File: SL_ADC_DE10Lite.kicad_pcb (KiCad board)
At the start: 4 copper layers, 98 x 67 mm, 23 parts, among them J1 DE10Lite header, J2 Analog header

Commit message: updated?
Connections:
- C5 pad 2: /DGND -> /AGND
- IC1 pad 24: /DGND -> /AGND
- J1 pad 12: /DGND -> /AGND
- J1 pad 30: /DGND -> /AGND
- J2 pad 27: /DGND -> /AGND
- J2 pad 28: /DGND -> /AGND
- J2 pad 5: unconnected-(J2-Pin_5-Pad5) -> /DVDD
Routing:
- net /AGND: track 82.6 -> 160.9 mm, vias 8 -> 26
- net /DGND: track 63.3 -> 0.00 mm, vias 3 -> 0
- net /DVDD: track 25.2 -> 77.2 mm, vias 1 -> 2
- added copper zone on In1.Cu, net /AGND
- removed copper zone on In1.Cu, net /DGND
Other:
- board text added: "DGND 3V3"
- board text removed: "DGND DVDD"

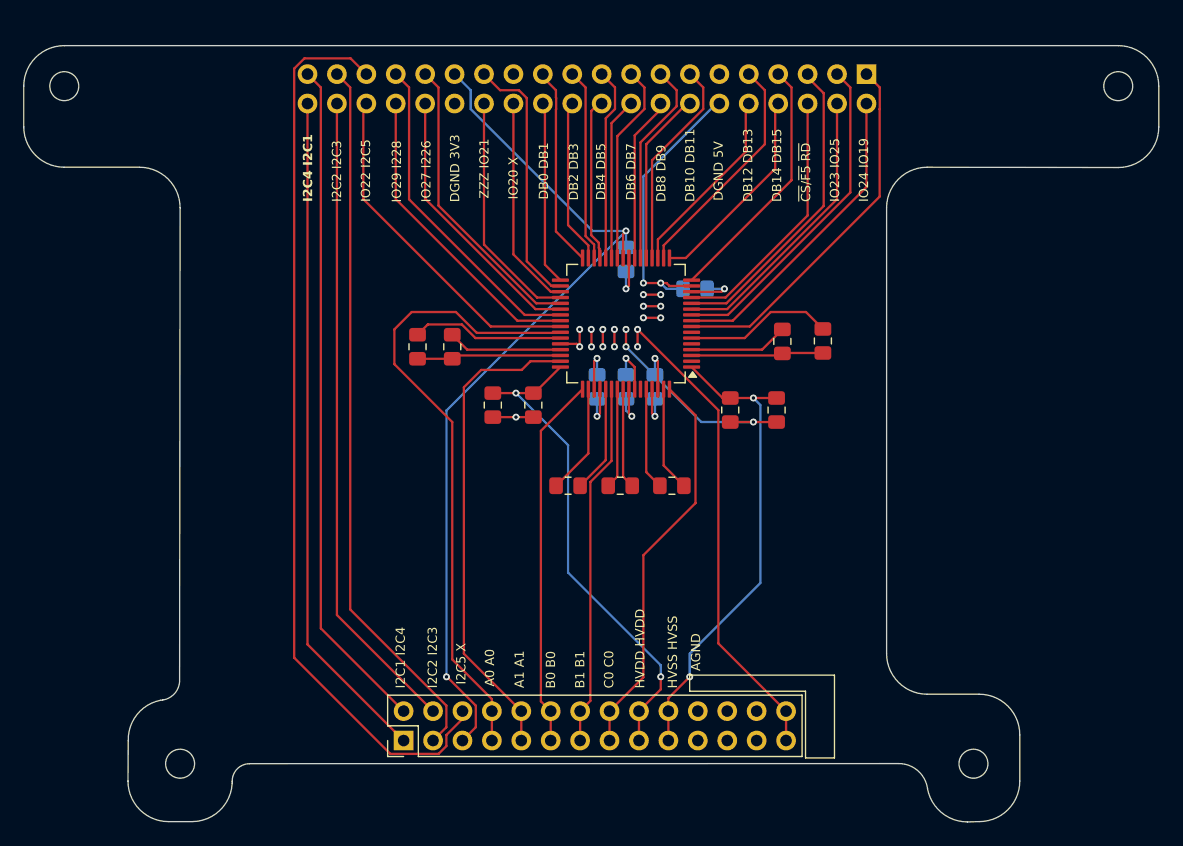
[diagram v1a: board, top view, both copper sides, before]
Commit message: widened standoff holes
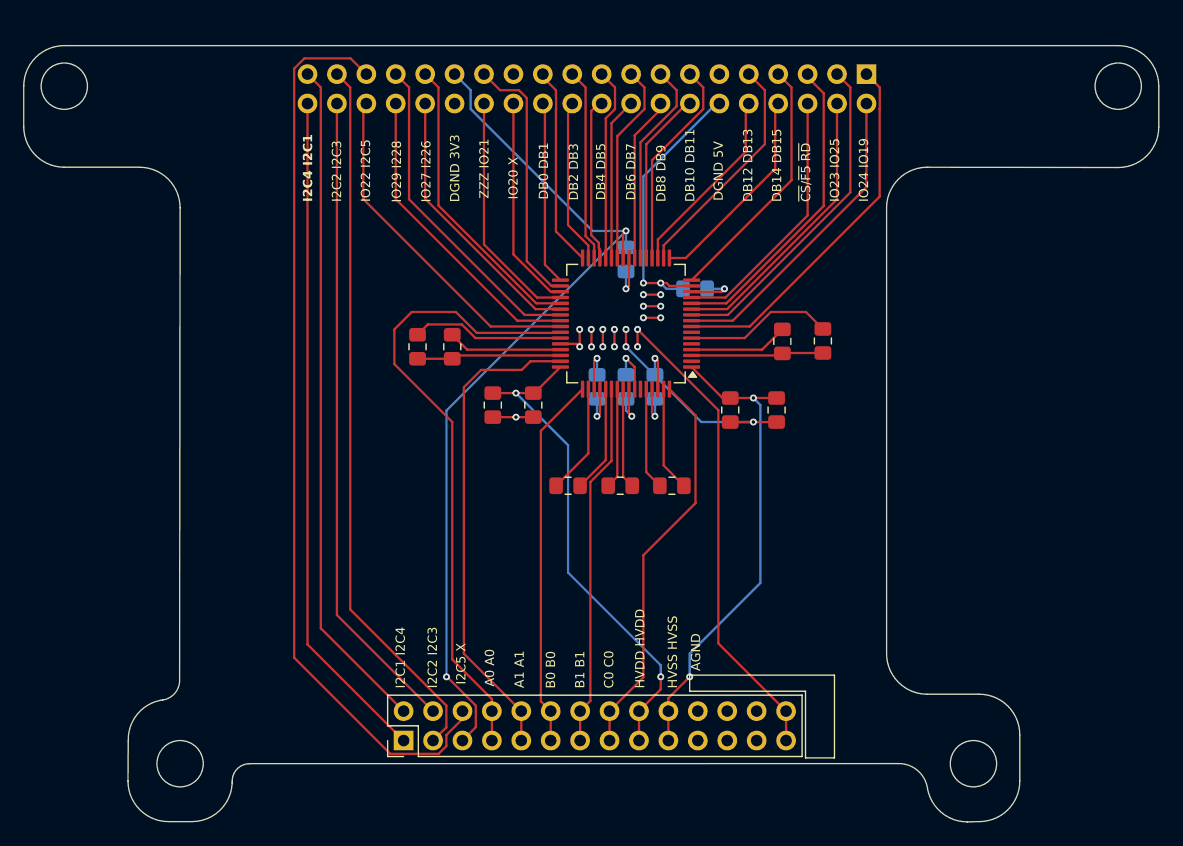
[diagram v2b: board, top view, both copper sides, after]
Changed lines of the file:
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@@
 		(pad "" np_thru_hole circle
 			(at 0 0)
-			(size 2.5 2.5)
-			(drill 2.5)
+			(size 4 4)
+			(drill 4)
 			(layers "*.Cu" "*.Mask")
 		)
@@
 		(pad "" np_thru_hole circle
 			(at 0 0)
-			(size 2.5 2.5)
-			(drill 2.5)
+			(size 4 4)
+			(drill 4)
 			(layers "*.Cu" "*.Mask")
 		)
@@
 		(pad "" np_thru_hole circle
 			(at 0 0)
-			(size 2.5 2.5)
-			(drill 2.5)
+			(size 4 4)
+			(drill 4)
 			(layers "*.Cu" "*.Mask")
 		)
@@
 		(pad "" np_thru_hole circle
 			(at 0 0)
-			(size 2.5 2.5)
-			(drill 2.5)
+			(size 4 4)
+			(drill 4)
 			(layers "*.Cu" "*.Mask")
 		)
@@
 	)
 	(segment
-		(start 83.35 102.85)
-		(end 83.35 51.983654)
+		(start 92.8 110)
+		(end 84.5 101.7)
 		(width 0.2)
 		(layer "F.Cu")
-		(net "/I2C5")
+		(net "/I2C4")
 	)
 	(segment
-		(start 88.22 51.1)
-		(end 89.58 52.46)
+		(start 84.5 101.7)
+		(end 84.5 55)
 		(width 0.2)
 		(layer "F.Cu")
-		(net "/I2C5")
+		(net "/I2C4")
 	)
 	(segment
-		(start 83.35 51.983654)
-		(end 84.233654 51.1)
+		(start 85.65 53.61)
+		(end 84.5 52.46)
 		(width 0.2)
 		(layer "F.Cu")
-		(net "/I2C5")
+		(net "/I2C1")
 	)
 	(segment
-		(start 96.49 110.476346)
-		(end 95.816346 111.15)
+		(start 92.8 107.46)
+		(end 85.65 100.31)
 		(width 0.2)
 		(layer "F.Cu")
-		(net "/I2C5")
+		(net "/I2C1")
 	)
 	(segment
-		(start 84.233654 51.1)
-		(end 88.22 51.1)
+		(start 85.65 100.31)
+		(end 85.65 53.61)
 		(width 0.2)
 		(layer "F.Cu")
-		(net "/I2C5")
+		(net "/I2C1")
 	)
 	(segment
-		(start 97.88 108.133654)
-		(end 96.49 109.523654)
+		(start 88.19 98.683654)
+		(end 88.19 53.61)
 		(width 0.2)
 		(layer "F.Cu")
-		(net "/I2C5")
+		(net "/I2C3")
 	)
 	(segment
-		(start 96.49 109.523654)
-		(end 96.49 110.476346)
+		(start 96.49 108.85)
+		(end 96.49 106.983654)
 		(width 0.2)
 		(layer "F.Cu")
-		(net "/I2C5")
+		(net "/I2C3")
 	)
 	(segment
-		(start 95.816346 111.15)
-		(end 91.65 111.15)
+		(start 95.34 110)
+		(end 96.49 108.85)
 		(width 0.2)
 		(layer "F.Cu")
-		(net "/I2C5")
+		(net "/I2C3")
 	)
 	(segment
-		(start 97.88 107.46)
-		(end 97.88 108.133654)
+		(start 96.49 106.983654)
+		(end 88.19 98.683654)
 		(width 0.2)
 		(layer "F.Cu")
-		(net "/I2C5")
+		(net "/I2C3")
 	)
 	(segment
-		(start 91.65 111.15)
-		(end 83.35 102.85)
+		(start 88.19 53.61)
+		(end 87.04 52.46)
 		(width 0.2)
 		(layer "F.Cu")
-		(net "/I2C5")
+		(net "/I2C3")
 	)
 	(segment
-		(start 92.8 110)
-		(end 84.5 101.7)
+		(start 95.34 107.46)
+		(end 87.04 99.16)
 		(width 0.2)
 		(layer "F.Cu")
-		(net "/I2C4")
+		(net "/I2C2")
 	)
 	(segment
-		(start 84.5 101.7)
-		(end 84.5 55)
+		(start 87.04 99.16)
+		(end 87.04 55)
 		(width 0.2)
 		(layer "F.Cu")
-		(net "/I2C4")
+		(net "/I2C2")
 	)
 	(segment
-		(start 88.19 98.683654)
-		(end 88.19 53.61)
+		(start 83.35 102.85)
+		(end 83.35 51.983654)
 		(width 0.2)
 		(layer "F.Cu")
-		(net "/I2C3")
+		(net "/I2C5")
 	)
 	(segment
-		(start 96.49 108.85)
-		(end 96.49 106.983654)
+		(start 88.22 51.1)
+		(end 89.58 52.46)
 		(width 0.2)
 		(layer "F.Cu")
-		(net "/I2C3")
+		(net "/I2C5")
 	)
 	(segment
-		(start 95.34 110)
-		(end 96.49 108.85)
+		(start 83.35 51.983654)
+		(end 84.233654 51.1)
 		(width 0.2)
 		(layer "F.Cu")
-		(net "/I2C3")
+		(net "/I2C5")
 	)
 	(segment
-		(start 96.49 106.983654)
-		(end 88.19 98.683654)
+		(start 96.49 110.476346)
+		(end 95.816346 111.15)
 		(width 0.2)
 		(layer "F.Cu")
-		(net "/I2C3")
+		(net "/I2C5")
 	)
 	(segment
-		(start 88.19 53.61)
-		(end 87.04 52.46)
+		(start 84.233654 51.1)
+		(end 88.22 51.1)
 		(width 0.2)
 		(layer "F.Cu")
-		(net "/I2C3")
+		(net "/I2C5")
 	)
 	(segment
-		(start 95.34 107.46)
-		(end 87.04 99.16)
+		(start 97.88 108.133654)
+		(end 96.49 109.523654)
 		(width 0.2)
 		(layer "F.Cu")
-		(net "/I2C2")
+		(net "/I2C5")
 	)
 	(segment
-		(start 87.04 99.16)
-		(end 87.04 55)
+		(start 96.49 109.523654)
+		(end 96.49 110.476346)
 		(width 0.2)
 		(layer "F.Cu")
-		(net "/I2C2")
+		(net "/I2C5")
 	)
 	(segment
-		(start 85.65 53.61)
-		(end 84.5 52.46)
+		(start 95.816346 111.15)
+		(end 91.65 111.15)
 		(width 0.2)
 		(layer "F.Cu")
-		(net "/I2C1")
+		(net "/I2C5")
 	)
 	(segment
-		(start 92.8 107.46)
-		(end 85.65 100.31)
+		(start 97.88 107.46)
+		(end 97.88 108.133654)
 		(width 0.2)
 		(layer "F.Cu")
-		(net "/I2C1")
+		(net "/I2C5")
 	)
 	(segment
-		(start 85.65 100.31)
-		(end 85.65 53.61)
+		(start 91.65 111.15)
+		(end 83.35 102.85)
 		(width 0.2)
 		(layer "F.Cu")
-		(net "/I2C1")
+		(net "/I2C5")
 	)
 	(zone

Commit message: Add graphics!
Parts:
- added ?: LOGO, PCBDrawings:Cloud, F.Cu at (79.0, 52.5)
- added ?: LOGO, PCBDrawings:Cloud, F.Cu at (127.0, 51.0)
- added ?: LOGO, PCBDrawings:SimpleFish, F.Cu at (89.5, 87.0)
- added ?: LOGO, PCBDrawings:SubbotsFish, F.Cu at (125.0, 91.5)
- added ?: LOGO, PCBDrawings:Mountains, F.Cu at (142.5, 105.5)
- added ?: LOGO, PCBDrawings:Cloud, F.Cu at (68.0, 59.5)
- added ?: LOGO, PCBDrawings:Cloud, F.Cu at (105.0, 54.0)
- added ?: LOGO, PCBDrawings:Mountains, F.Cu at (82.5, 104.5)
- added ?: LOGO, PCBDrawings:Cloud, F.Cu at (143.0, 55.0)
- added G: LOGO, PCBDrawings:SubbotsLogo, F.Cu at (83.5, 72.5)
- moved J2 6.00 mm to (92.8, 104.0)
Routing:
- net /AGND: track 160.9 -> 122.6 mm
- net /I2C5: track 78.5 -> 72.3 mm
- net /I2C3: track 61.9 -> 55.9 mm
- net /I2C4: track 58.4 -> 52.4 mm
- net /I2C2: track 55.9 -> 49.9 mm
- net /I2C1: track 58.4 -> 52.4 mm
- net /HVSS: track 41.6 -> 35.6 mm
- net /HVDD: track 42.7 -> 36.7 mm
- net /DVDD: track 77.2 -> 71.2 mm
- net /CH_C0: track 34.3 -> 28.3 mm
- net /CH_B1: track 31.5 -> 25.5 mm
- net /CH_B0: track 32.2 -> 26.2 mm
- net /CH_A1: track 41.8 -> 35.8 mm
- net /CH_A0: track 54.4 -> 48.4 mm
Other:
- outline, holes or cut-outs redrawn

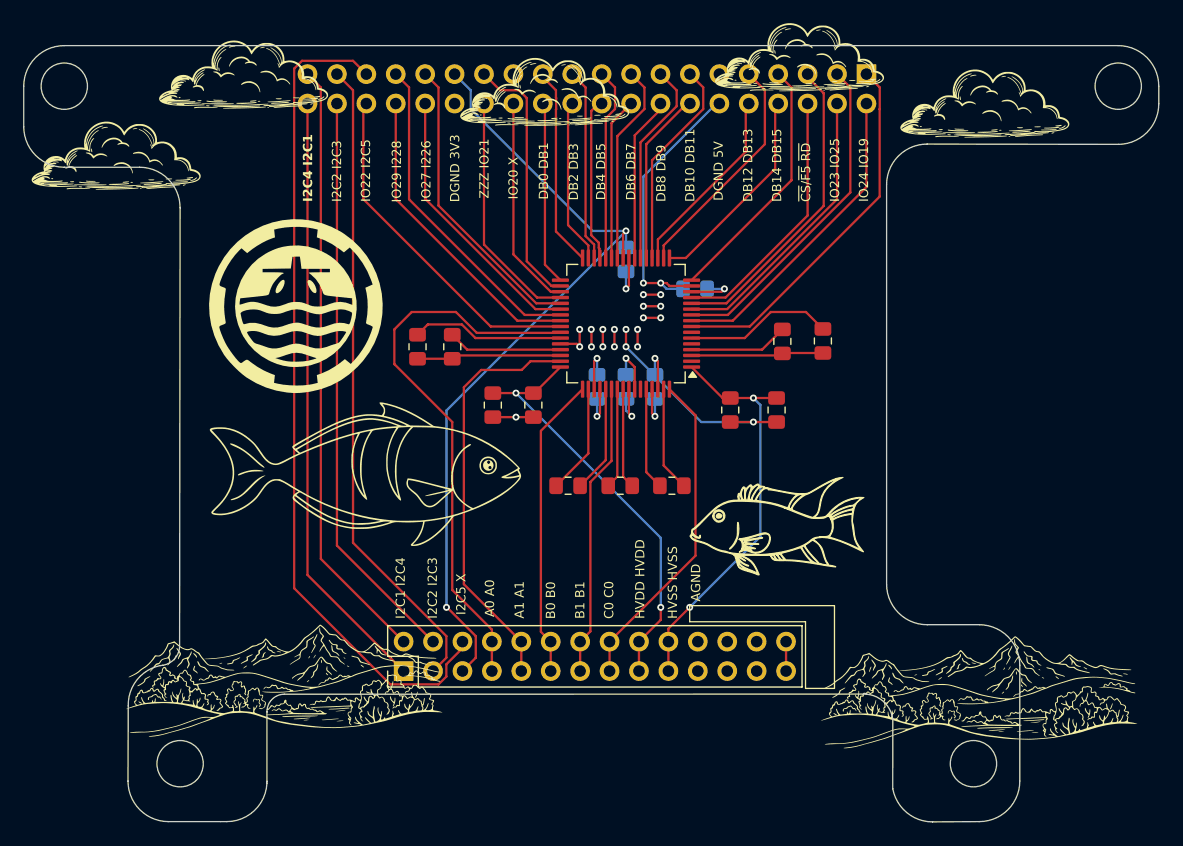
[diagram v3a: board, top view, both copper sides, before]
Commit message: added a few ground vias and fixed board outline error
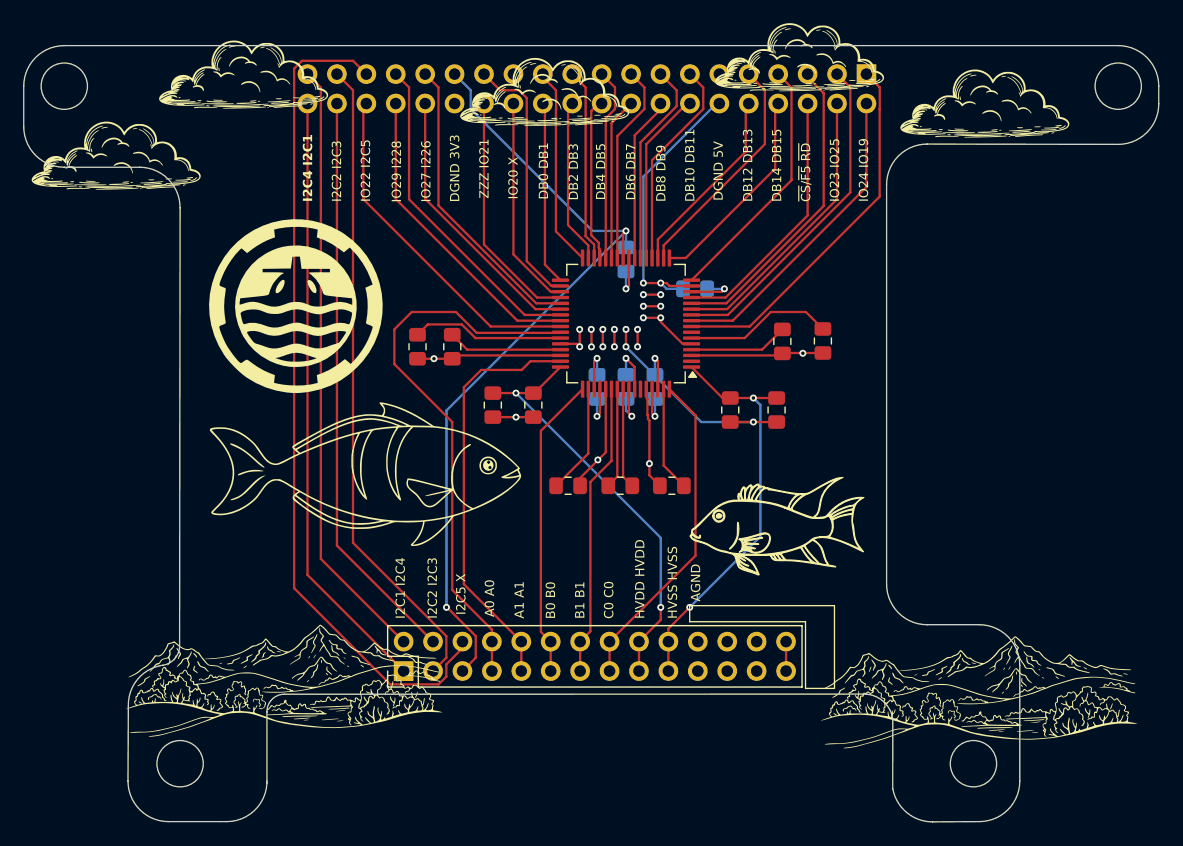
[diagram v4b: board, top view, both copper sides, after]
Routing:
- net /AGND: track 122.6 -> 126.4 mm, vias 26 -> 30
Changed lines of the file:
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@@
 	(gr_line
 		(start 69 113.5)
-		(end 69.022543 107.000278)
-		(stroke
-			(width 0.1)
-			(type solid)
-		)
-		(layer "Edge.Cuts")
-	)
-	(gr_arc
-		(start 69.022543 107.000278)
-		(mid 69.778755 104.755964)
-		(end 71.801578 103.524302)
+		(end 69.030968 107.005976)
+		(stroke
+			(width 0.1)
+			(type solid)
+		)
+		(layer "Edge.Cuts")
+	)
+	(gr_arc
+		(start 69.030968 107.005976)
+		(mid 69.787179 104.761662)
+		(end 71.81 103.53)
 		(stroke
 			(width 0.1)
@@
 	(gr_line
 		(start 72 103.5)
-		(end 71.803412 103.533458)
+		(end 71.81 103.53)
 		(stroke
 			(width 0.1)
@@
 	)
 	(segment
+		(start 114.02 82.368529)
+		(end 113.9 82.248529)
+		(width 0.2)
+		(layer "F.Cu")
+		(net "/AGND")
+	)
+	(segment
+		(start 113.9 81.965686)
+		(end 113.85 81.915685)
+		(width 0.2)
+		(layer "F.Cu")
+		(net "/AGND")
+	)
+	(segment
 		(start 109.017961 74.517961)
 		(end 109 74.5)
@@
 	)
 	(segment
+		(start 115 73.85741)
+		(end 115 73.5)
+		(width 0.2)
+		(layer "F.Cu")
+		(net "/AGND")
+	)
+	(segment
 		(start 112 77)
 		(end 112.75 77.75)
@@
 	)
 	(segment
+		(start 113.8 79.7125)
+		(end 113.75 79.6625)
+		(width 0.2)
+		(layer "F.Cu")
+		(net "/AGND")
+	)
+	(segment
 		(start 102.5 82.075)
 		(end 100.5 82.075)
@@
 	)
 	(segment
-		(start 110.25 85.7875)
-		(end 110.25 79.6625)
+		(start 108.0375 88)
+		(end 108.0375 87.3325)
 		(width 0.2)
 		(layer "F.Cu")
@@
 	)
 	(segment
-		(start 113.75 86.825)
-		(end 113.75 79.6625)
-		(width 0.2)
-		(layer "F.Cu")
-		(net "/AGND")
-	)
-	(segment
-		(start 114.925 88)
-		(end 113.75 86.825)
+		(start 113.8 80.48241)
+		(end 113.8 79.7125)
+		(width 0.2)
+		(layer "F.Cu")
+		(net "/AGND")
+	)
+	(segment
+		(start 117.6625 75.75)
+		(end 116.89259 75.75)
+		(width 0.2)
+		(layer "F.Cu")
+		(net "/AGND")
+	)
+	(segment
+		(start 114.02 87.095)
+		(end 114.02 82.368529)
 		(width 0.2)
 		(layer "F.Cu")
@@
 	)
 	(segment
+		(start 116.89259 75.75)
+		(end 115 73.85741)
+		(width 0.2)
+		(layer "F.Cu")
+		(net "/AGND")
+	)
+	(segment
+		(start 113.85 81.915685)
+		(end 113.85 80.53241)
+		(width 0.2)
+		(layer "F.Cu")
+		(net "/AGND")
+	)
+	(segment
+		(start 113.85 80.53241)
+		(end 113.8 80.48241)
+		(width 0.2)
+		(layer "F.Cu")
+		(net "/AGND")
+	)
+	(segment
 		(start 112.75 77.75)
 		(end 112.75 79.6625)
@@
 	)
 	(segment
+		(start 110.25 85.12)
+		(end 110.25 79.6625)
+		(width 0.2)
+		(layer "F.Cu")
+		(net "/AGND")
+	)
+	(segment
 		(start 113 76)
 		(end 113 74.5)
@@
 	)
 	(segment
+		(start 114.925 88)
+		(end 114.02 87.095)
+		(width 0.2)
+		(layer "F.Cu")
+		(net "/AGND")
+	)
+	(segment
 		(start 97.2875 76.75)
 		(end 106.3375 76.75)
@@
 	)
 	(segment
-		(start 108.0375 88)
-		(end 110.25 85.7875)
+		(start 108.0375 87.3325)
+		(end 110.25 85.12)
 		(width 0.2)
 		(layer "F.Cu")
@@
 		(net "/AGND")
 	)
+	(segment
+		(start 113.9 82.248529)
+		(end 113.9 81.965686)
+		(width 0.2)
+		(layer "F.Cu")
+		(net "/AGND")
+	)
+	(via
+		(at 127.27 76.56)
+		(size 0.6)
+		(drill 0.3)
+		(layers "F.Cu" "B.Cu")
+		(net "/AGND")
+	)
 	(via
 		(at 113 76)
@@
 	)
 	(via
+		(at 114.02 86.09)
+		(size 0.6)
+		(drill 0.3)
+		(layers "F.Cu" "B.Cu")
+		(net "/AGND")
+	)
+	(via
 		(at 109 74.5)
 		(size 0.6)
@@
 	)
 	(via
+		(at 95.42 77.03)
+		(size 0.6)
+		(drill 0.3)
+		(layers "F.Cu" "B.Cu")
+		(net "/AGND")
+	)
+	(via
 		(at 115 70.5)
 		(size 0.6)
@@
 		(net "/AGND")
 	)
+	(via
+		(at 109.57 85.77)
+		(size 0.6)
+		(drill 0.3)
+		(layers "F.Cu" "B.Cu")
+		(net "/AGND")
+	)
